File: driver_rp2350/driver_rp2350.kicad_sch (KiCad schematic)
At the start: 0 parts

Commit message: Worked on rp2350 schematic.
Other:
- added sheet drivers (drivers.kicad_sch)
- sheet panel_leds ports: added COL_0, COL_1, COL_2, COL_3, COL_4, COL_5, COL_6, COL_7, COL_8, COL_9, COL_A, COL_B, COL_C, COL_D, COL_E, COL_F, ROW_0, ROW_1, ROW_2, ROW_3, ROW_4, ROW_5, ROW_6, ROW_7, ROW_8, ROW_9, ROW_A, ROW_B, ROW_C, ROW_D, ROW_E, ROW_F; removed none
- sheet panel_mcu ports: added COL_MCU_0; removed CS0

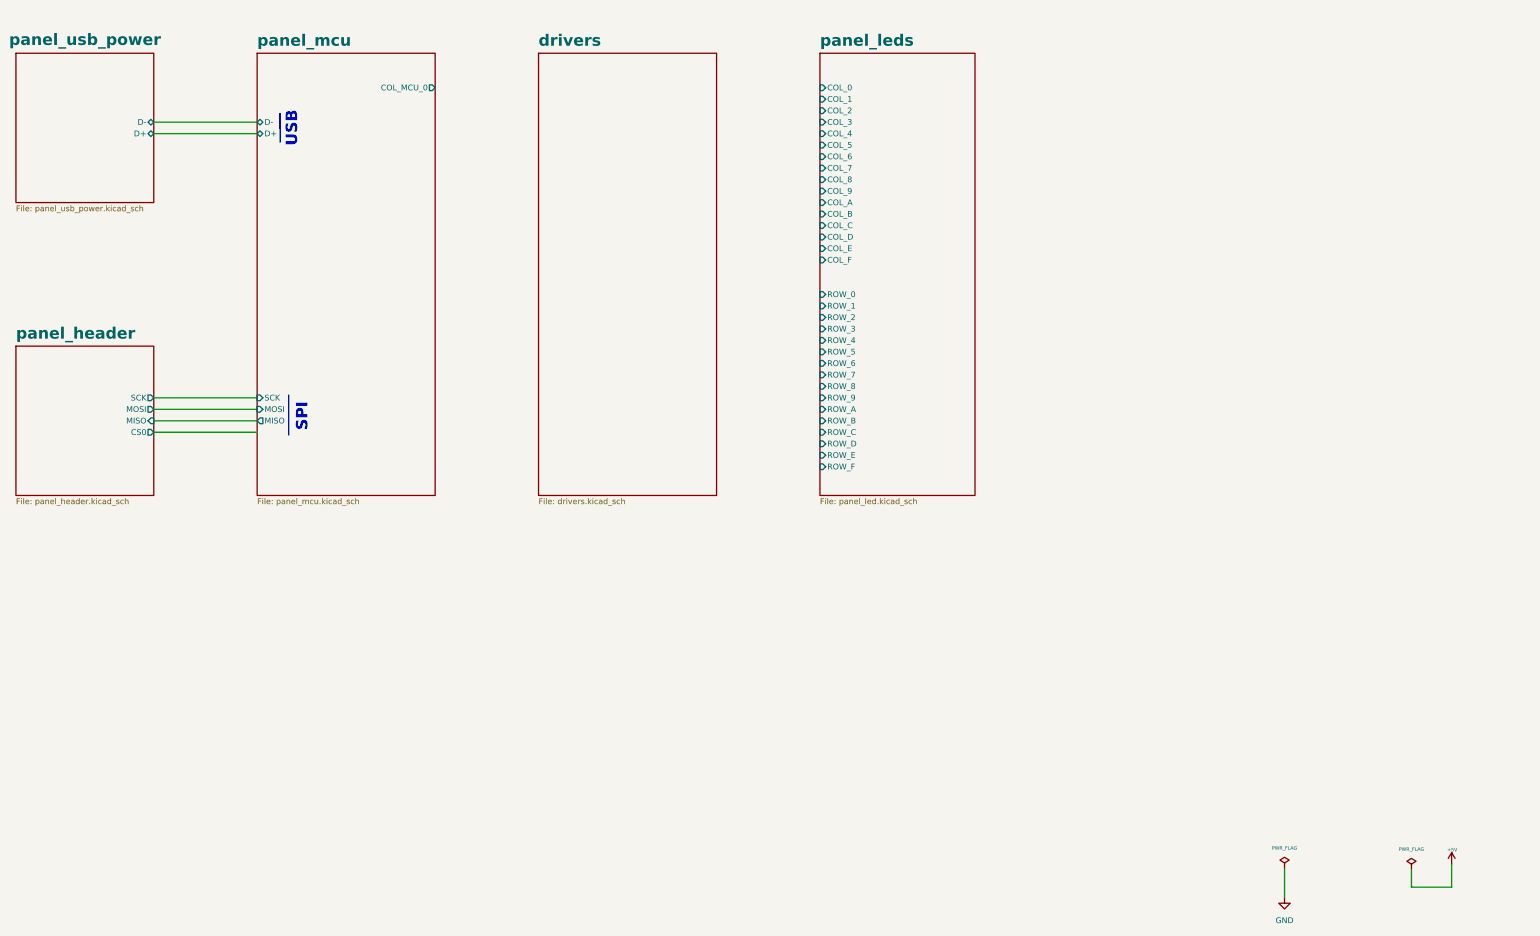
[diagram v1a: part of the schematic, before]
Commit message: Finished first version of schematic for rp2350 G6 panel.
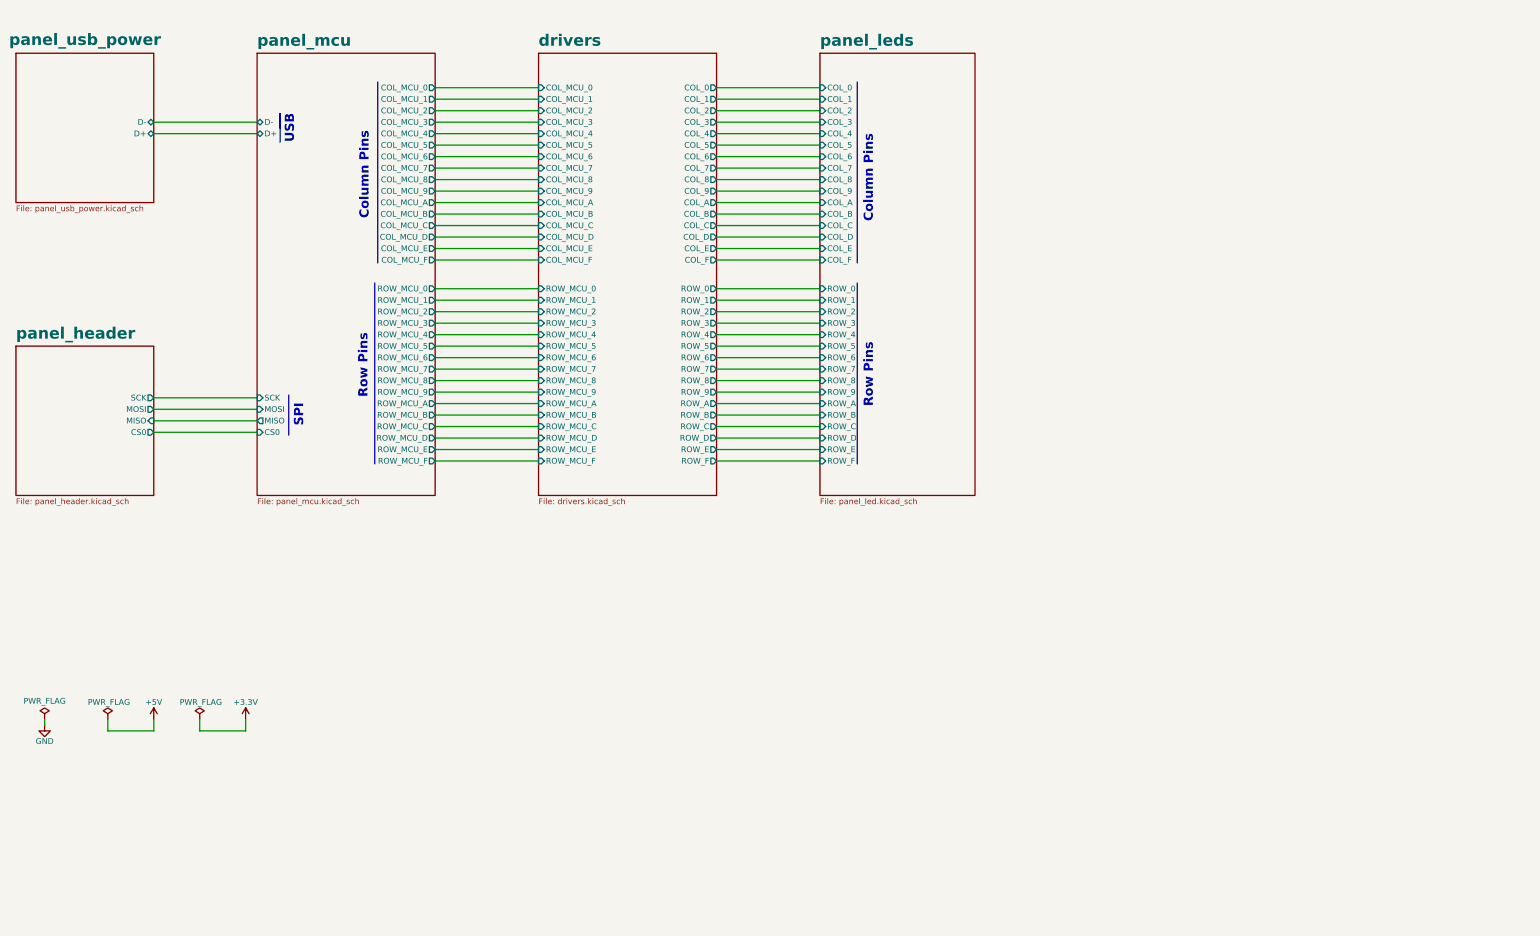
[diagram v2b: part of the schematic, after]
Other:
- sheet drivers ports: added COL_0, COL_1, COL_2, COL_3, COL_4, COL_5, COL_6, COL_7, COL_8, COL_9, COL_A, COL_B, COL_C, COL_D, COL_E, COL_F, COL_MCU_0, COL_MCU_1, COL_MCU_2, COL_MCU_3, COL_MCU_4, COL_MCU_5, COL_MCU_6, COL_MCU_7, COL_MCU_8, COL_MCU_9, COL_MCU_A, COL_MCU_B, COL_MCU_C, COL_MCU_D, COL_MCU_E, COL_MCU_F, ROW_0, ROW_1, ROW_2, ROW_3, ROW_4, ROW_5, ROW_6, ROW_7, ROW_8, ROW_9, ROW_A, ROW_B, ROW_C, ROW_D, ROW_E, ROW_F, ROW_MCU_0, ROW_MCU_1, ROW_MCU_2, ROW_MCU_3, ROW_MCU_4, ROW_MCU_5, ROW_MCU_6, ROW_MCU_7, ROW_MCU_8, ROW_MCU_9, ROW_MCU_A, ROW_MCU_B, ROW_MCU_C, ROW_MCU_D, ROW_MCU_E, ROW_MCU_F; removed none
- sheet panel_mcu ports: added COL_MCU_1, COL_MCU_2, COL_MCU_3, COL_MCU_4, COL_MCU_5, COL_MCU_6, COL_MCU_7, COL_MCU_8, COL_MCU_9, COL_MCU_A, COL_MCU_B, COL_MCU_C, COL_MCU_D, COL_MCU_E, COL_MCU_F, CS0, ROW_MCU_0, ROW_MCU_1, ROW_MCU_2, ROW_MCU_3, ROW_MCU_4, ROW_MCU_5, ROW_MCU_6, ROW_MCU_7, ROW_MCU_8, ROW_MCU_9, ROW_MCU_A, ROW_MCU_B, ROW_MCU_C, ROW_MCU_D, ROW_MCU_E, ROW_MCU_F; removed none
- note added: "Column Pins"
- note added: "Row Pins"
